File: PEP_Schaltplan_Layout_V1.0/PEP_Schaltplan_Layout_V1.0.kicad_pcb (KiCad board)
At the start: 2 copper layers, 202.5 x 119.7 mm, 140 parts, among them J1 Conn_01x02_Pin, J10 Conn_01x01_Pin, J11 Conn_01x02_Pin, J12 Conn_01x01_Pin, J2 Conn_01x01_Pin, J3 Conn_01x01_Pin, J4 Conn_01x01_Pin, J5 Conn_01x01_Pin, J6 Conn_01x01_Pin, J7 Conn_01x01_Pin, J8 Conn_01x01_Pin, J9 Conn_01x01_Pin, Q1 BC546, Q2 BC556, SW1 SW_DIP_x04, SW10 SW_DIP_x04, SW11 SW_DIP_x04, SW12 SW_DIP_x04, SW13 SW_DIP_x04, SW14 SW_DIP_x04, SW15 SW_DIP_x04, SW16 SW_DIP_x04, SW2 SW_DIP_x04, SW3 SW_DIP_x04, SW4 SW_DIP_x04, SW5 SW_DIP_x04, SW6 SW_DIP_x04, SW7 SW_DIP_x04, SW8 SW_DIP_x04, SW9 SW_DIP_x04, U1 AD822ANZ_new, U2 LM7805_TO220, U3 LM7905_TO220, U4 LT1819, U5 LT1819, U6 LT1819, U7 LT1819

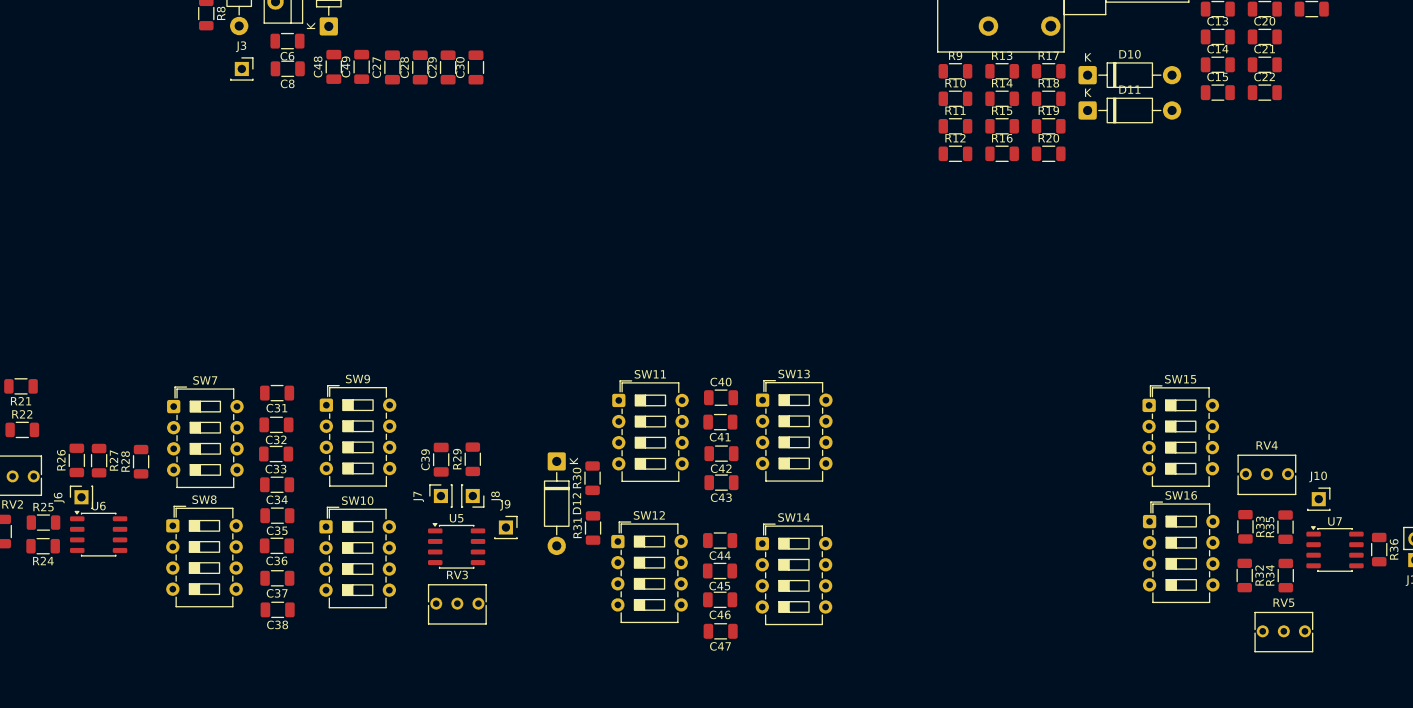
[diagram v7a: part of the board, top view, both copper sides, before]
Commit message: ic Kondensator
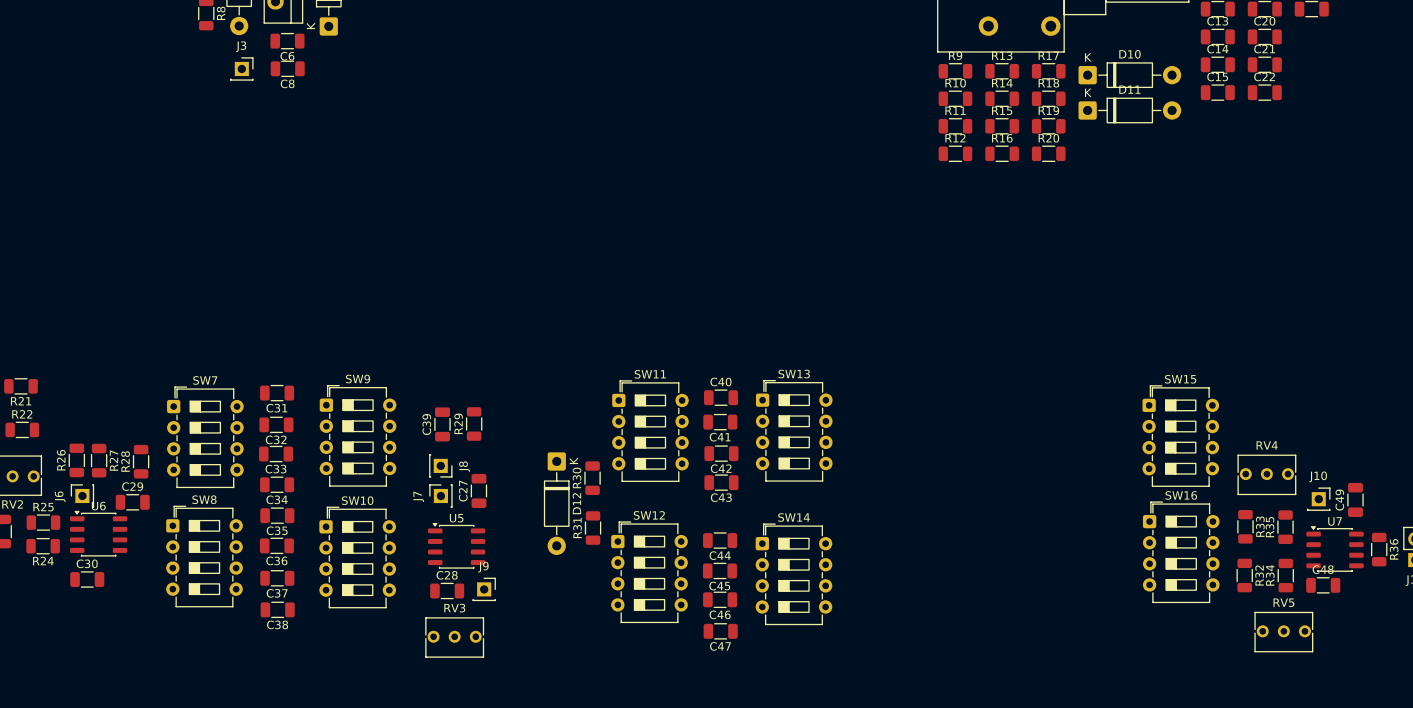
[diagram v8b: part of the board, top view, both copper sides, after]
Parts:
- moved C48 134.4 mm to (228.5, 144.4), turned to 0 degrees
- moved C49 130.4 mm to (232.4, 134.1)
- moved C30 77.4 mm to (79.8, 143.7), turned to 0 degrees
- moved C29 64.6 mm to (85.3, 134.4), turned to 0 degrees
- moved C28 63.1 mm to (123.1, 145.1), turned to 0 degrees
- moved C27 52.0 mm to (126.9, 133.1)
- moved J9 7.89 mm to (127.5, 144.9)
- moved J8 5.29 mm to (122.3, 130.0)
- moved R29 4.25 mm to (126.3, 125.0)
- moved C39 4.25 mm to (122.5, 125.0)
- moved RV3 4.00 mm to (126.5, 150.6)
- moved J6 0.20 mm to (79.2, 133.7)
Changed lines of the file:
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@@
 	(footprint "Connector_PinSocket_2.54mm:PinSocket_1x01_P2.54mm_Vertical"
 		(layer "F.Cu")
-		(at 126.173559 133.662726 -90)
+		(at 122.323559 130.040226 -90)
 		(descr "Through hole straight socket strip, 1x01, 2.54mm pitch, single row (from Kicad 4.0.7), script generated")
 		(tags "Through hole socket strip THT 1x01 2.54mm single row")
@@
 	(footprint "Connector_PinSocket_2.54mm:PinSocket_1x01_P2.54mm_Vertical"
 		(layer "F.Cu")
-		(at 130.158559 137.452726)
+		(at 127.543559 144.900226)
 		(descr "Through hole straight socket strip, 1x01, 2.54mm pitch, single row (from Kicad 4.0.7), script generated")
 		(tags "Through hole socket strip THT 1x01 2.54mm single row")
@@
 	(footprint "Capacitor_SMD:C_1206_3216Metric"
 		(layer "F.Cu")
-		(at 126.553559 82.100226 90)
+		(at 79.783559 143.710226)
 		(descr "Capacitor SMD 1206 (3216 Metric), square (rectangular) end terminal, IPC-7351 nominal, (Body size source: IPC-SM-782 page 76, https://www.pcb-3d.com/wordpress/wp-content/uploads/ipc-sm-782a_amendment_1_and_2.pdf)")
 		(tags "capacitor")
 		(property "Reference" "C30"
-			(at 0 -1.85 90)
+			(at 0 -1.85 0)
 			(layer "F.SilkS")
 			(effects
@@
 		)
 		(property "Value" "100n"
-			(at 0 1.85 90)
+			(at 0 1.85 0)
 			(layer "F.Fab")
 			(effects
@@
 		)
 		(property "Datasheet" ""
-			(at 0 0 90)
+			(at 0 0 0)
 			(layer "F.Fab")
 			(hide yes)
@@
 		)
 		(property "Description" ""
-			(at 0 0 90)
+			(at 0 0 0)
 			(layer "F.Fab")
 			(hide yes)
@@
 		)
 		(property "Sim.Device" "C"
-			(at 0 0 90)
+			(at 0 0 0)
 			(unlocked yes)
 			(layer "F.Fab")
@@
 		)
 		(property "Sim.Params" "C=100n"
-			(at 0 0 90)
+			(at 0 0 0)
 			(unlocked yes)
 			(layer "F.Fab")
@@
 		)
 		(fp_text user "${REFERENCE}"
-			(at 0 0 90)
+			(at 0 0 0)
 			(layer "F.Fab")
 			(effects
@@
 		)
 		(pad "1" smd roundrect
-			(at -1.475 0 90)
+			(at -1.475 0)
 			(size 1.15 1.8)
 			(layers "F.Cu" "F.Mask" "F.Paste")
@@
 		)
 		(pad "2" smd roundrect
-			(at 1.475 0 90)
+			(at 1.475 0)
 			(size 1.15 1.8)
 			(layers "F.Cu" "F.Mask" "F.Paste")
@@
 	(footprint "Connector_PinSocket_2.54mm:PinSocket_1x01_P2.54mm_Vertical"
 		(layer "F.Cu")
-		(at 79.088559 133.817726 90)
+		(at 79.203559 133.660226 90)
 		(descr "Through hole straight socket strip, 1x01, 2.54mm pitch, single row (from Kicad 4.0.7), script generated")
 		(tags "Through hole socket strip THT 1x01 2.54mm single row")
@@
 	(footprint "Potentiometer_THT:Potentiometer_Bourns_3266Y_Vertical"
 		(layer "F.Cu")
-		(at 126.853559 146.612726)
+		(at 126.533559 150.600226)
 		(descr "Potentiometer, vertical, Bourns 3266Y, https://www.bourns.com/docs/Product-Datasheets/3266.pdf")
 		(tags "Potentiometer vertical Bourns 3266Y")
@@
 	(footprint "Capacitor_SMD:C_1206_3216Metric"
 		(layer "F.Cu")
-		(at 123.203559 82.100226 90)
+		(at 85.253559 134.420226)
 		(descr "Capacitor SMD 1206 (3216 Metric), square (rectangular) end terminal, IPC-7351 nominal, (Body size source: IPC-SM-782 page 76, https://www.pcb-3d.com/wordpress/wp-content/uploads/ipc-sm-782a_amendment_1_and_2.pdf)")
 		(tags "capacitor")
 		(property "Reference" "C29"
-			(at 0 -1.85 90)
+			(at 0 -1.85 0)
 			(layer "F.SilkS")
 			(effects
@@
 		)
 		(property "Value" "100n"
-			(at 0 1.85 90)
+			(at 0 1.85 0)
 			(layer "F.Fab")
 			(effects
@@
 		)
 		(property "Datasheet" ""
-			(at 0 0 90)
+			(at 0 0 0)
 			(layer "F.Fab")
 			(hide yes)
@@
 		)
 		(property "Description" ""
-			(at 0 0 90)
+			(at 0 0 0)
 			(layer "F.Fab")
 			(hide yes)
@@
 		)
 		(property "Sim.Device" "C"
-			(at 0 0 90)
+			(at 0 0 0)
 			(unlocked yes)
 			(layer "F.Fab")
@@
 		)
 		(property "Sim.Params" "C=100n"
-			(at 0 0 90)
+			(at 0 0 0)
 			(unlocked yes)
 			(layer "F.Fab")
@@
 		)
 		(fp_text user "${REFERENCE}"
-			(at 0 0 90)
+			(at 0 0 0)
 			(layer "F.Fab")
 			(effects
@@
 		)
 		(pad "1" smd roundrect
-			(at -1.475 0 90)
+			(at -1.475 0)
 			(size 1.15 1.8)
 			(layers "F.Cu" "F.Mask" "F.Paste")
@@
 		)
 		(pad "2" smd roundrect
-			(at 1.475 0 90)
+			(at 1.475 0)
 			(size 1.15 1.8)
 			(layers "F.Cu" "F.Mask" "F.Paste")
@@
 	(footprint "Capacitor_SMD:C_1206_3216Metric"
 		(layer "F.Cu")
-		(at 109.448559 82.030226 90)
+		(at 228.503559 144.410226)
 		(descr "Capacitor SMD 1206 (3216 Metric), square (rectangular) end terminal, IPC-7351 nominal, (Body size source: IPC-SM-782 page 76, https://www.pcb-3d.com/wordpress/wp-content/uploads/ipc-sm-782a_amendment_1_and_2.pdf)")
 		(tags "capacitor")
 		(property "Reference" "C48"
-			(at 0 -1.85 90)
+			(at 0 -1.85 0)
 			(layer "F.SilkS")
 			(effects
@@
 		)
 		(property "Value" "100n"
-			(at 0 1.85 90)
+			(at 0 1.85 0)
 			(layer "F.Fab")
 			(effects
@@
 		)
 		(property "Datasheet" ""
-			(at 0 0 90)
+			(at 0 0 0)
 			(layer "F.Fab")
 			(hide yes)
@@
 		)
 		(property "Description" ""
-			(at 0 0 90)
+			(at 0 0 0)
 			(layer "F.Fab")
 			(hide yes)
@@
 		)
 		(property "Sim.Device" "C"
-			(at 0 0 90)
+			(at 0 0 0)
 			(unlocked yes)
 			(layer "F.Fab")
@@
 		)
 		(property "Sim.Params" "C=100n"
-			(at 0 0 90)
+			(at 0 0 0)
 			(unlocked yes)
 			(layer "F.Fab")
@@
 		)
 		(fp_text user "${REFERENCE}"
-			(at 0 0 90)
+			(at 0 0 0)
 			(layer "F.Fab")
 			(effects
@@
 		)
 		(pad "1" smd roundrect
-			(at -1.475 0 90)
+			(at -1.475 0)
 			(size 1.15 1.8)
 			(layers "F.Cu" "F.Mask" "F.Paste")
@@
 		)
 		(pad "2" smd roundrect
-			(at 1.475 0 90)
+			(at 1.475 0)
 			(size 1.15 1.8)
 			(layers "F.Cu" "F.Mask" "F.Paste")
@@
 	(footprint "Capacitor_SMD:C_1206_3216Metric"
 		(layer "F.Cu")
-		(at 112.798559 82.030226 90)
+		(at 232.383559 134.140226 90)
 		(descr "Capacitor SMD 1206 (3216 Metric), square (rectangular) end terminal, IPC-7351 nominal, (Body size source: IPC-SM-782 page 76, https://www.pcb-3d.com/wordpress/wp-content/uploads/ipc-sm-782a_amendment_1_and_2.pdf)")
 		(tags "capacitor")
@@
 	(footprint "Capacitor_SMD:C_1206_3216Metric"
 		(layer "F.Cu")
-		(at 122.368559 129.292726 90)
+		(at 122.528559 125.047726 90)
 		(descr "Capacitor SMD 1206 (3216 Metric), square (rectangular) end terminal, IPC-7351 nominal, (Body size source: IPC-SM-782 page 76, https://www.pcb-3d.com/wordpress/wp-content/uploads/ipc-sm-782a_amendment_1_and_2.pdf)")
 		(tags "capacitor")
@@
 	(footprint "Capacitor_SMD:C_1206_3216Metric"
 		(layer "F.Cu")
-		(at 116.503559 82.100226 90)
+		(at 126.913559 133.055226 90)
 		(descr "Capacitor SMD 1206 (3216 Metric), square (rectangular) end terminal, IPC-7351 nominal, (Body size source: IPC-SM-782 page 76, https://www.pcb-3d.com/wordpress/wp-content/uploads/ipc-sm-782a_amendment_1_and_2.pdf)")
 		(tags "capacitor")
@@
 	(footprint "Capacitor_SMD:C_1206_3216Metric"
 		(layer "F.Cu")
-		(at 119.853559 82.100226 90)
+		(at 123.093559 145.090226)
 		(descr "Capacitor SMD 1206 (3216 Metric), square (rectangular) end terminal, IPC-7351 nominal, (Body size source: IPC-SM-782 page 76, https://www.pcb-3d.com/wordpress/wp-content/uploads/ipc-sm-782a_amendment_1_and_2.pdf)")
 		(tags "capacitor")
 		(property "Reference" "C28"
-			(at 0 -1.85 90)
+			(at 0 -1.85 0)
 			(layer "F.SilkS")
 			(effects
@@
 		)
 		(property "Value" "100n"
-			(at 0 1.85 90)
+			(at 0 1.85 0)
 			(layer "F.Fab")
 			(effects
@@
 		)
 		(property "Datasheet" ""
-			(at 0 0 90)
+			(at 0 0 0)
 			(layer "F.Fab")
 			(hide yes)
@@
 		)
 		(property "Description" ""
-			(at 0 0 90)
+			(at 0 0 0)
 			(layer "F.Fab")
 			(hide yes)
@@
 		)
 		(property "Sim.Device" "C"
-			(at 0 0 90)
+			(at 0 0 0)
 			(unlocked yes)
 			(layer "F.Fab")
@@
 		)
 		(property "Sim.Params" "C=100n"
-			(at 0 0 90)
+			(at 0 0 0)
 			(unlocked yes)
 			(layer "F.Fab")
@@
 		)
 		(fp_text user "${REFERENCE}"
-			(at 0 0 90)
+			(at 0 0 0)
 			(layer "F.Fab")
 			(effects
@@
 		)
 		(pad "1" smd roundrect
-			(at -1.475 0 90)
+			(at -1.475 0)
 			(size 1.15 1.8)
 			(layers "F.Cu" "F.Mask" "F.Paste")
@@
 		)
 		(pad "2" smd roundrect
-			(at 1.475 0 90)
+			(at 1.475 0)
 			(size 1.15 1.8)
 			(layers "F.Cu" "F.Mask" "F.Paste")
@@
 	(footprint "Resistor_SMD:R_1206_3216Metric"
 		(layer "F.Cu")
-		(at 126.173559 129.242726 90)
+		(at 126.333559 124.997726 90)
 		(descr "Resistor SMD 1206 (3216 Metric), square (rectangular) end terminal, IPC-7351 nominal, (Body size source: IPC-SM-782 page 72, https://www.pcb-3d.com/wordpress/wp-content/uploads/ipc-sm-782a_amendment_1_and_2.pdf)")
 		(tags "resistor")
